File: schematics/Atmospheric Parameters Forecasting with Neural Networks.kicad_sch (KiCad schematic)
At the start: 3 parts, among them U1 DHT11, U2 BMP180

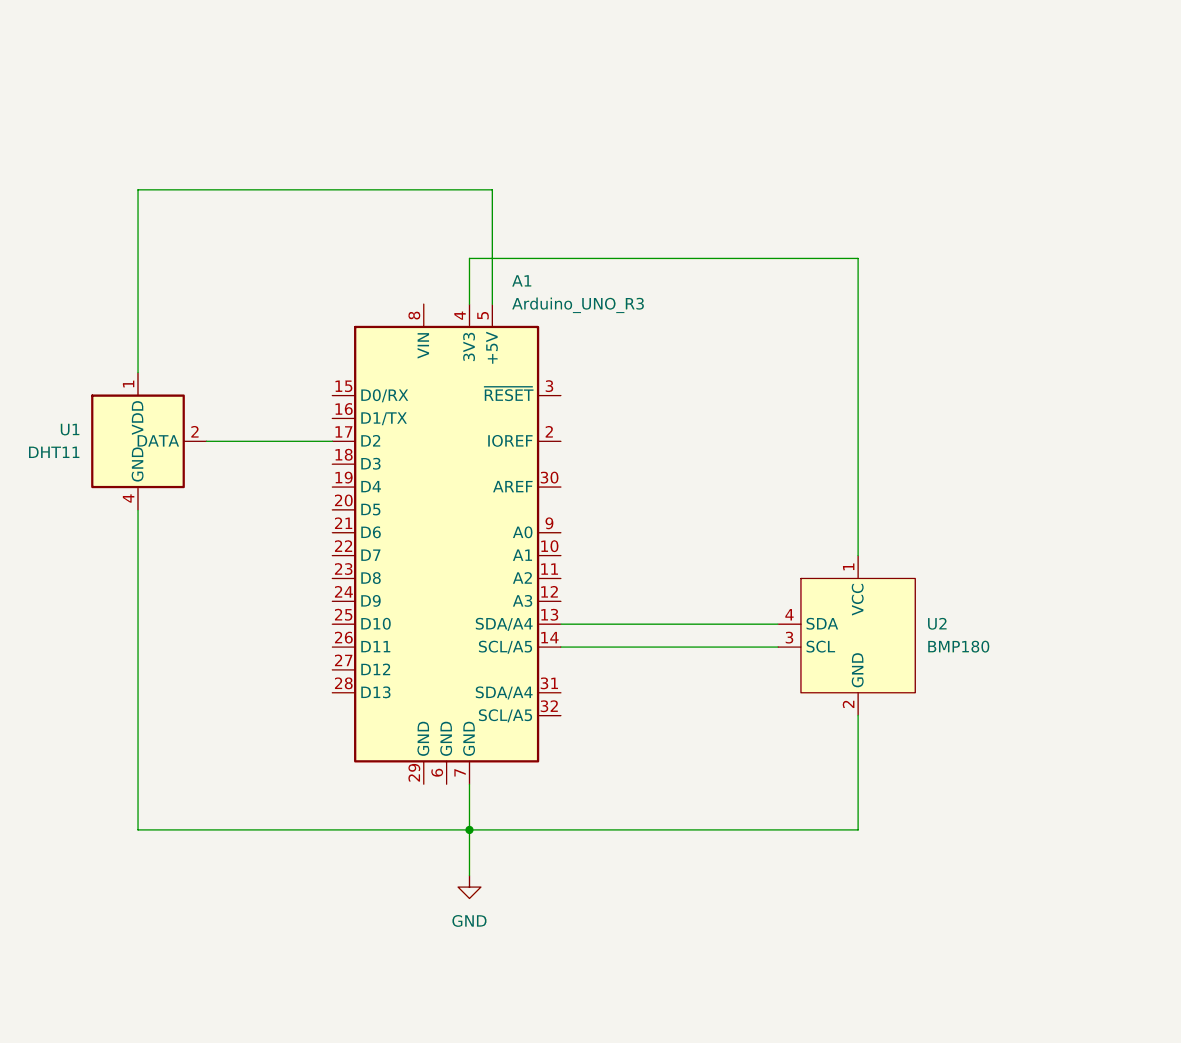
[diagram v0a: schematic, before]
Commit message: added BH1750, MQ-2, MQ-135, Analogue Anemometer and Wind Direction sensors support
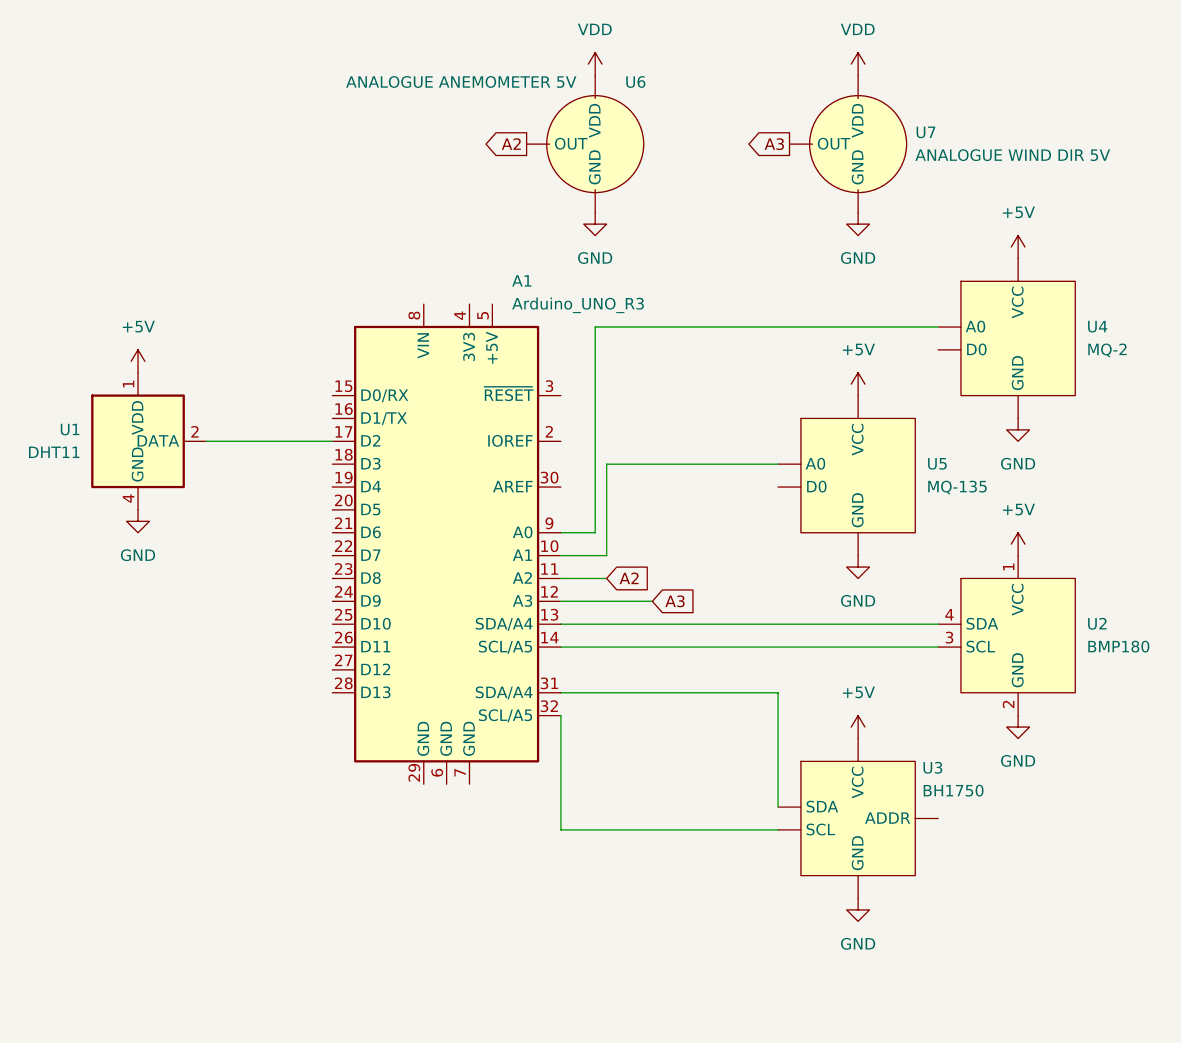
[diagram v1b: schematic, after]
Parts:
- removed U2: BMP180, symbol maurg1975_bmp180:BMP180
- added U2: BMP180, symbol maurg1975_sensors:BMP180
- added U3: BH1750, symbol maurg1975_sensors:BH1750
- added U4: MQ-2, symbol maurg1975_sensors:MQ-2
- added U5: MQ-135, symbol maurg1975_sensors:MQ-135
- added U6: ANALOGUE ANEMOMETER 5V, symbol maurg1975_sensors:ANEMOMETER_ANALOGUE
- added U7: ANALOGUE WIND DIR 5V, symbol maurg1975_sensors:WIND_DIR_ANALOGUE
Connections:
- net GND: now also U2.2 (GND), U3. (VCC), U4. (VCC), U5. (VCC), U6. (VDD), U7. (VDD); no longer A1.7 (GND)
- net at A1.5 (+5V): no longer U1.1 (VDD)
- net at A1.14 (SCL/A5): now also U2.3 (SCL)
- net at A1.13 (SDA/A4): now also U2.4 (SDA)
- net at A1.10 (A1): now also U5. (VCC)
- net A2: now reaches A1.11 (A2)
- net A2: now also U6. (VDD)
- net A3: now reaches A1.12 (A3)
- net A3: now also U7. (VDD)
- net at A1.31 (SDA/A4): now also U3. (VCC)
- net at A1.32 (SCL/A5): now also U3. (VCC)
- net at A1.9 (A0): now also U4. (VCC)
- new net +5V: U1.1 (VDD), U2.1 (VCC), U3. (VCC), U4. (VCC), U5. (VCC)
- new net VDD: U6. (VDD), U7. (VDD)

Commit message: sensor connections on the Arduino board have been changed; 2 plots per row are displayed
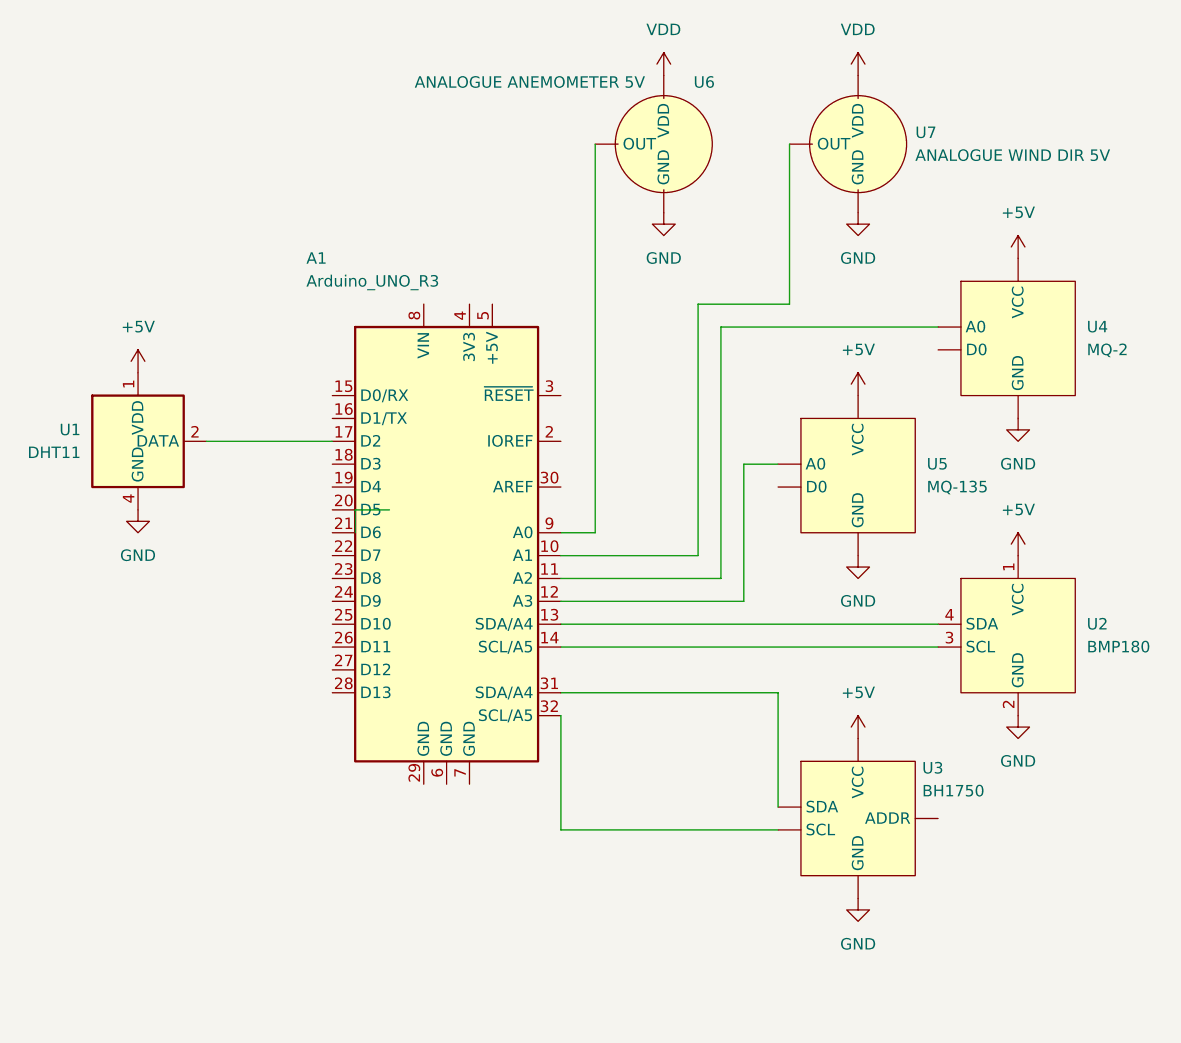
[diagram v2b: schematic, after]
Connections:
- net at A1.9 (A0): now also U6. (VDD); no longer U4. (VCC)
- net at A1.10 (A1): now also U7. (VDD); no longer U5. (VCC)
- net A2: no longer names the net of A1.11 (A2)
- net A2: now also U4. (VCC); no longer U6. (VDD)
- net A3: no longer names the net of A1.12 (A3)
- net A3: now also U5. (VCC); no longer U7. (VDD)
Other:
- moved on the sheet: U6
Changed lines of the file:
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@@
 	(wire
 		(pts
-			(xy 149.86 106.68) (xy 160.02 106.68)
-		)
-		(stroke
-			(width 0)
-			(type default)
-		)
-	)
-	(wire
-		(pts
-			(xy 154.94 91.44) (xy 154.94 101.6)
-		)
-		(stroke
-			(width 0)
-			(type default)
-		)
-	)
-	(wire
-		(pts
-			(xy 153.67 76.2) (xy 153.67 99.06)
-		)
-		(stroke
-			(width 0)
-			(type default)
-		)
-	)
-	(wire
-		(pts
-			(xy 173.99 91.44) (xy 154.94 91.44)
+			(xy 149.86 101.6) (xy 165.1 101.6)
+		)
+		(stroke
+			(width 0)
+			(type default)
+		)
+	)
+	(wire
+		(pts
+			(xy 165.1 73.66) (xy 165.1 101.6)
+		)
+		(stroke
+			(width 0)
+			(type default)
+		)
+	)
+	(wire
+		(pts
+			(xy 175.26 55.88) (xy 175.26 73.66)
+		)
+		(stroke
+			(width 0)
+			(type default)
+		)
+	)
+	(wire
+		(pts
+			(xy 170.18 91.44) (xy 170.18 106.68)
+		)
+		(stroke
+			(width 0)
+			(type default)
+		)
+	)
+	(wire
+		(pts
+			(xy 167.64 76.2) (xy 167.64 104.14)
+		)
+		(stroke
+			(width 0)
+			(type default)
+		)
+	)
+	(wire
+		(pts
+			(xy 175.26 73.66) (xy 165.1 73.66)
+		)
+		(stroke
+			(width 0)
+			(type default)
+		)
+	)
+	(wire
+		(pts
+			(xy 173.99 91.44) (xy 170.18 91.44)
+		)
+		(stroke
+			(width 0)
+			(type default)
+		)
+	)
+	(wire
+		(pts
+			(xy 170.18 106.68) (xy 149.86 106.68)
 		)
 		(stroke
@@
 	(wire
 		(pts
-			(xy 149.86 99.06) (xy 153.67 99.06)
-		)
-		(stroke
-			(width 0)
-			(type default)
-		)
-	)
-	(wire
-		(pts
 			(xy 173.99 116.84) (xy 149.86 116.84)
 		)
@@
 	(wire
 		(pts
-			(xy 149.86 104.14) (xy 154.94 104.14)
+			(xy 153.67 55.88) (xy 153.67 99.06)
 		)
 		(stroke
@@
 	(wire
 		(pts
-			(xy 154.94 101.6) (xy 149.86 101.6)
+			(xy 167.64 104.14) (xy 149.86 104.14)
 		)
 		(stroke
@@
 	(wire
 		(pts
+			(xy 153.67 99.06) (xy 149.86 99.06)
+		)
+		(stroke
+			(width 0)
+			(type default)
+		)
+	)
+	(wire
+		(pts
+			(xy 127 96.52) (xy 127 99.06)
+		)
+		(stroke
+			(width 0)
+			(type default)
+		)
+	)
+	(wire
+		(pts
+			(xy 130.81 96.52) (xy 127 96.52)
+		)
+		(stroke
+			(width 0)
+			(type default)
+		)
+	)
+	(wire
+		(pts
 			(xy 173.99 132.08) (xy 149.86 132.08)
 		)
@@
 	(wire
 		(pts
-			(xy 191.77 76.2) (xy 153.67 76.2)
-		)
-		(stroke
-			(width 0)
-			(type default)
-		)
-	)
-	(global_label "A3"
-		(shape input)
-		(at 160.02 106.68 0)
-		(fields_autoplaced yes)
-		(effects
-			(font
-				(size 1.27 1.27)
-			)
-			(justify left)
-		)
-		(property "Intersheetrefs" "${INTERSHEET_REFS}"
-			(at 165.3033 106.68 0)
-			(effects
-				(font
-					(size 1.27 1.27)
-				)
-				(justify left)
-				(hide yes)
-			)
-		)
-	)
-	(global_label "A2"
-		(shape output)
-		(at 146.05 55.88 180)
-		(fields_autoplaced yes)
-		(effects
-			(font
-				(size 1.27 1.27)
-			)
-			(justify right)
-		)
-		(property "Intersheetrefs" "${INTERSHEET_REFS}"
-			(at 140.7667 55.88 0)
-			(effects
-				(font
-					(size 1.27 1.27)
-				)
-				(justify right)
-				(hide yes)
-			)
-		)
-	)
-	(global_label "A3"
-		(shape output)
-		(at 175.26 55.88 180)
-		(fields_autoplaced yes)
-		(effects
-			(font
-				(size 1.27 1.27)
-			)
-			(justify right)
-		)
-		(property "Intersheetrefs" "${INTERSHEET_REFS}"
-			(at 169.9767 55.88 0)
-			(effects
-				(font
-					(size 1.27 1.27)
-				)
-				(justify right)
-				(hide yes)
-			)
-		)
-	)
-	(global_label "A2"
-		(shape input)
-		(at 154.94 104.14 0)
-		(fields_autoplaced yes)
-		(effects
-			(font
-				(size 1.27 1.27)
-			)
-			(justify left)
-		)
-		(property "Intersheetrefs" "${INTERSHEET_REFS}"
-			(at 160.2233 104.14 0)
-			(effects
-				(font
-					(size 1.27 1.27)
-				)
-				(justify left)
-				(hide yes)
-			)
+			(xy 191.77 76.2) (xy 167.64 76.2)
+		)
+		(stroke
+			(width 0)
+			(type default)
 		)
 	)
@@
 	(symbol
 		(lib_id "maurg1975_sensors:ANEMOMETER_ANALOGUE")
-		(at 153.67 55.88 0)
+		(at 161.29 55.88 0)
 		(unit 1)
 		(exclude_from_sim no)
@@
 		(dnp no)
 		(property "Reference" "U6"
-			(at 156.972 49.022 0)
+			(at 164.592 49.022 0)
 			(effects
 				(font
@@
 		)
 		(property "Value" "ANALOGUE ANEMOMETER 5V"
-			(at 125.984 49.022 0)
+			(at 133.604 49.022 0)
 			(effects
 				(font
@@
 		)
 		(property "Footprint" ""
-			(at 153.67 55.88 0)
-			(effects
-				(font
-					(size 1.27 1.27)
-				)
-				(hide yes)
-			)
-		)
-		(property "Datasheet" ""
-			(at 153.67 55.88 0)
+			(at 161.29 55.88 0)
+			(effects
+				(font
+					(size 1.27 1.27)
+				)
+				(hide yes)
+			)
+		)
+		(property "Datasheet" ""
+			(at 161.29 55.88 0)
 			(effects
 				(font
@@
 		)
 		(property "Description" ""
-			(at 153.67 55.88 0)
+			(at 161.29 55.88 0)
 			(effects
 				(font
@@
 	(symbol
 		(lib_id "power:VDD")
-		(at 153.67 48.26 0)
+		(at 161.29 48.26 0)
 		(unit 1)
 		(exclude_from_sim no)
@@
 		(fields_autoplaced yes)
 		(property "Reference" "#PWR013"
-			(at 153.67 52.07 0)
+			(at 161.29 52.07 0)
 			(effects
 				(font
@@
 		)
 		(property "Value" "VDD"
-			(at 153.67 43.18 0)
-			(effects
-				(font
-					(size 1.27 1.27)
-				)
-			)
-		)
-		(property "Footprint" ""
-			(at 153.67 48.26 0)
-			(effects
-				(font
-					(size 1.27 1.27)
-				)
-				(hide yes)
-			)
-		)
-		(property "Datasheet" ""
-			(at 153.67 48.26 0)
+			(at 161.29 43.18 0)
+			(effects
+				(font
+					(size 1.27 1.27)
+				)
+			)
+		)
+		(property "Footprint" ""
+			(at 161.29 48.26 0)
+			(effects
+				(font
+					(size 1.27 1.27)
+				)
+				(hide yes)
+			)
+		)
+		(property "Datasheet" ""
+			(at 161.29 48.26 0)
 			(effects
 				(font
@@
 		)
 		(property "Description" "Power symbol creates a global label with name \"VDD\""
-			(at 153.67 48.26 0)
+			(at 161.29 48.26 0)
 			(effects
 				(font
@@
 		(on_board yes)
 		(dnp no)
-		(fields_autoplaced yes)
 		(property "Reference" "A1"
-			(at 144.4341 71.12 0)
+			(at 121.5741 68.58 0)
 			(effects
 				(font
@@
 		)
 		(property "Value" "Arduino_UNO_R3"
-			(at 144.4341 73.66 0)
+			(at 121.5741 71.12 0)
 			(effects
 				(font
@@
 	(symbol
 		(lib_id "power:GND")
-		(at 153.67 63.5 0)
+		(at 161.29 63.5 0)
 		(unit 1)
 		(exclude_from_sim no)
@@
 		(fields_autoplaced yes)
 		(property "Reference" "#PWR012"
-			(at 153.67 69.85 0)
+			(at 161.29 69.85 0)
 			(effects
 				(font
@@
 		)
 		(property "Value" "GND"
-			(at 153.67 68.58 0)
-			(effects
-				(font
-					(size 1.27 1.27)
-				)
-			)
-		)
-		(property "Footprint" ""
-			(at 153.67 63.5 0)
-			(effects
-				(font
-					(size 1.27 1.27)
-				)
-				(hide yes)
-			)
-		)
-		(property "Datasheet" ""
-			(at 153.67 63.5 0)
+			(at 161.29 68.58 0)
+			(effects
+				(font
+					(size 1.27 1.27)
+				)
+			)
+		)
+		(property "Footprint" ""
+			(at 161.29 63.5 0)
+			(effects
+				(font
+					(size 1.27 1.27)
+				)
+				(hide yes)
+			)
+		)
+		(property "Datasheet" ""
+			(at 161.29 63.5 0)
 			(effects
 				(font
@@
 		)
 		(property "Description" "Power symbol creates a global label with name \"GND\" , ground"
-			(at 153.67 63.5 0)
-			(effects
-				(font
+			(at 161.29 63.5 0)
+			(effects
+				(font

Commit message: added rain sensor support and changed plots visualization layout
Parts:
- removed A1: Arduino_UNO_R3, Module:Arduino_UNO_R3, symbol MCU_Module:Arduino_UNO_R3
- added A2: Arduino_Nano_v3.x, Module:Arduino_Nano, symbol MCU_Module:Arduino_Nano_v3.x
- added U8: RAIN SENSOR, symbol maurg1975_sensors:RAIN_SENSOR
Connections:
- net +5V: now also U8. (VCC)
- net GND: now also U8. (VCC)
- net at U1.2 (DATA): now also A2.5 (D2)
- net at U2.3 (SCL): now also U3. (VCC), A2.24 (A5)
- net at U2.4 (SDA): now also U3. (VCC), A2.23 (A4)
- new net: A2.20 (A1), U7. (VDD)
- new net: A2.21 (A2), U4. (VCC)
- new net: A2.19 (A0), U6. (VDD)
- new net: A2.22 (A3), U5. (VCC)
- new net: A2.25 (A6), U8. (VCC)
